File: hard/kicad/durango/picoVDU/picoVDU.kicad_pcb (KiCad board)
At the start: 2 copper layers, 31 parts, among them J1 VIDEO, Q1 BC547B, Q2 BC547B, U1 74HCT93, U10 74HC21, U11 74HC20, U12 74HCT02, U13 74HCT00, U14 74HC175, U15 74HC86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

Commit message: improved picoVDU
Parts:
- added J2: IOX, Connector_PinHeader_2.54mm:PinHeader_2x08_P2.54mm_Vertical, F.Cu at (11.4, 45.7)
- added U19: 74HC32, Package_DIP:DIP-14_W7.62mm_Socket, F.Cu at (4.48, 45.9)
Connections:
- net Net-(U15-Pad3) renamed /ABE
- U15 pad 1: ~ABE -> +5V
- U15 pad 2: +5V -> ~ABE
- U18 pad 1: /Interface/~IO8U -> /Interface/~SEL
- U18 pad 15: /Interface/~IO8Q -> /Interface/~DSEL
- U6 pad 12: Net-(U6-Pad12) -> GND

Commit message: routing picoVDU
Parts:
- J1: footprint Connector_Audio:Jack_3.5mm_Neutrik_NMJ6HCD2_Horizontal -> Connector_Coaxial:SMA_Amphenol_132289_EdgeMount
- moved U19 191.1 mm to (148.6, 171.4), turned to 90 degrees
- moved J2 182.6 mm to (170.2, 135.9)
- moved U6 174.3 mm to (137.2, 143.5), turned to 270 degrees
- moved J1 157.4 mm to (61.0, 174.0), turned to 180 degrees
- moved U13 142.1 mm to (88.9, 151.1), turned to 90 degrees
- moved U9 140.7 mm to (100.3, 171.4)
- moved U7 138.2 mm to (102.9, 184.2), turned to 90 degrees
- moved U15 136.5 mm to (148.6, 184.2), turned to 90 degrees
- moved U18 134.5 mm to (146.1, 158.8), turned to 90 degrees
- moved U14 130.0 mm to (125.7, 184.2), turned to 90 degrees
- moved R4 128.0 mm to (88.9, 171.4)
- moved U1 127.5 mm to (63.5, 133.3), turned to 180 degrees
- moved U12 126.3 mm to (128.3, 171.4), turned to 90 degrees
- moved C2 125.5 mm to (73.7, 174.0), turned to 180 degrees
- moved U8 122.2 mm to (68.6, 151.1), turned to 90 degrees
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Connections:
- J2 pad 10: D1 -> D4
- J2 pad 11: D2 -> /Interface/~SEL
- J2 pad 12: D3 -> D5
- J2 pad 13: D4 -> /Interface/~WE
- J2 pad 14: D5 -> D6
- J2 pad 15: D6 -> GND
- J2 pad 2: /Interface/A0 -> D0
- J2 pad 3: /Interface/A1 -> /Interface/A0
- J2 pad 4: /Interface/A2 -> D1
- J2 pad 5: /Interface/A3 -> /Interface/A1
- J2 pad 6: /Interface/~SEL -> D2
- J2 pad 7: /Interface/~WE -> /Interface/A2
- J2 pad 8: GND -> D3
- J2 pad 9: D0 -> /Interface/A3
- U17 pad 12: INV -> Net-(U17-Pad12)
- U17 pad 16: Net-(U17-Pad16) -> INV
- U3 pad 10: Net-(U10-Pad8) -> Net-(U13-Pad12)
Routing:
- net GND: track 0.00 -> 441.6 mm, vias 0 -> 2
- net +5V: track 0.00 -> 378.9 mm
- net INV: track 0.00 -> 72.7 mm, vias 0 -> 2
- net ~ABE: track 0.00 -> 47.8 mm, vias 0 -> 1
- net /VD1: track 0.00 -> 47.1 mm, vias 0 -> 2
- net /Interface/A1: track 0.00 -> 41.8 mm, vias 0 -> 1
- net D7: track 0.00 -> 37.7 mm
- net D0: track 0.00 -> 37.5 mm
- net /VD2: track 0.00 -> 36.6 mm
- net Net-(U17-Pad11): track 0.00 -> 35.7 mm
- net D6: track 0.00 -> 35.1 mm
- net D1: track 0.00 -> 33.9 mm, vias 0 -> 1
- net Net-(U11-Pad9): track 0.00 -> 32.6 mm
- net D5: track 0.00 -> 28.8 mm, vias 0 -> 1
- net /VD7: track 0.00 -> 28.0 mm
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
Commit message: more routing on picoVDU
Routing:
- net Net-(U10-Pad4): track 0.00 -> 129.7 mm, vias 0 -> 4
- net Net-(U10-Pad12): track 0.00 -> 107.1 mm, vias 0 -> 2
- net +5V: track 378.9 -> 482.4 mm, vias 0 -> 3
- net Net-(U10-Pad2): track 0.00 -> 93.7 mm, vias 0 -> 3
- net Net-(R3-Pad2): track 0.00 -> 82.2 mm
- net Net-(U10-Pad1): track 0.00 -> 79.5 mm, vias 0 -> 2
- net D4: track 26.6 -> 104.2 mm, vias 1 -> 3
- net ~DBE: track 0.00 -> 72.6 mm, vias 0 -> 1
- net D3: track 22.6 -> 93.5 mm, vias 1 -> 3
- net D5: track 28.8 -> 97.1 mm, vias 1 -> 2
- net D2: track 25.7 -> 94.1 mm, vias 1 -> 3
- net VA9: track 0.00 -> 67.5 mm, vias 0 -> 2
- net /Interface/~SEL: track 8.67 -> 74.1 mm, vias 0 -> 2
- net D0: track 37.5 -> 101.4 mm, vias 0 -> 1
- net VA10: track 0.00 -> 62.4 mm, vias 0 -> 2
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
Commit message: almost routed picoVDU
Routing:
- net Net-(U12-Pad5): track 0.00 -> 142.3 mm, vias 0 -> 5
- net Net-(U10-Pad5): track 13.8 -> 137.5 mm, vias 0 -> 5
- net Net-(U13-Pad12): track 0.00 -> 123.5 mm, vias 0 -> 4
- net /ABE: track 13.8 -> 130.1 mm, vias 0 -> 4
- net Net-(U1-Pad8): track 0.00 -> 114.7 mm
- net Net-(U11-Pad13): track 0.00 -> 92.8 mm, vias 0 -> 1
- net Net-(U14-Pad9): track 47.4 -> 113.0 mm, vias 1 -> 2
- net Net-(U11-Pad1): track 0.00 -> 64.9 mm, vias 0 -> 2
- net Net-(U2-Pad9): track 0.00 -> 64.1 mm, vias 0 -> 2
- net Net-(U1-Pad2): track 0.00 -> 60.7 mm, vias 0 -> 3
- net Net-(U13-Pad2): track 11.2 -> 66.4 mm, vias 0 -> 1
- net GND: track 468.2 -> 509.2 mm, vias 2 -> 5
- net VA5: track 33.3 -> 73.9 mm, vias 1 -> 4
- net Net-(U10-Pad9): track 14.8 -> 52.2 mm, vias 0 -> 2
- net Net-(U11-Pad9): track 32.6 -> 69.2 mm, vias 0 -> 2
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
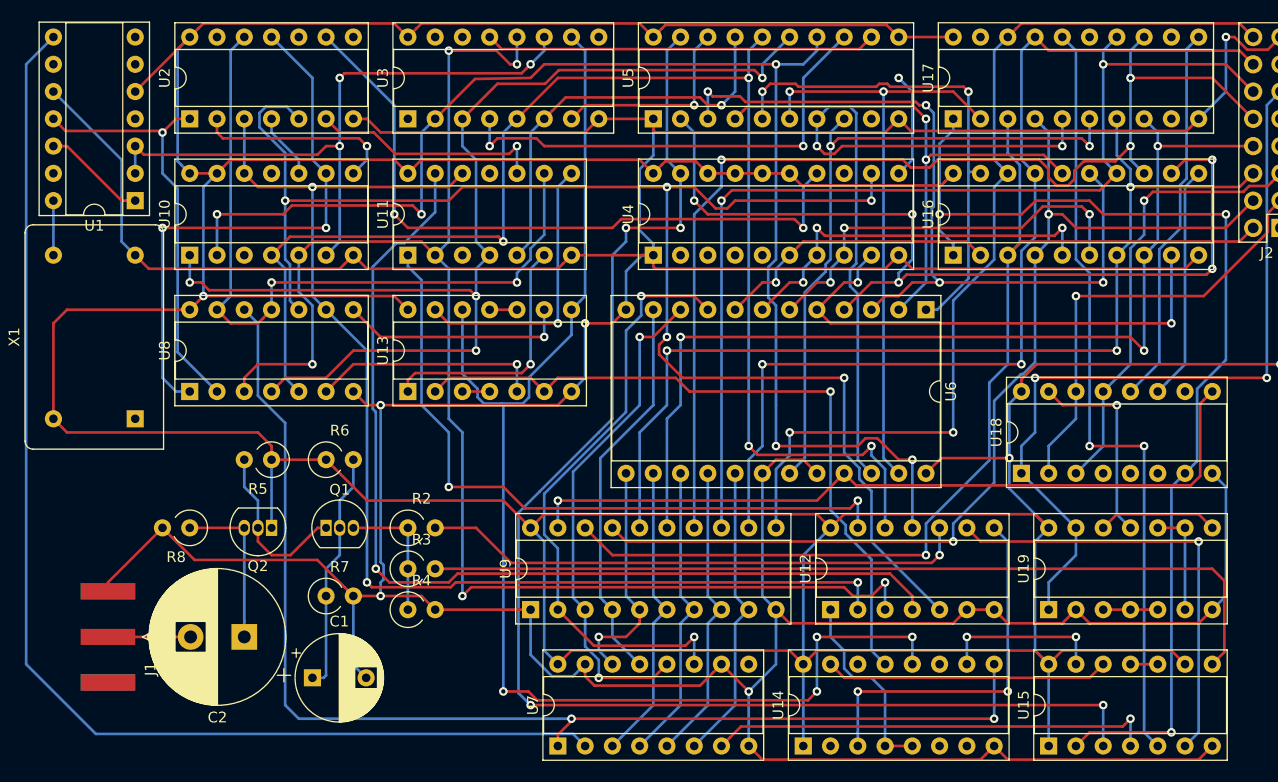
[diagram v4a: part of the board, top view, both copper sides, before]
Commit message: finished routing picoVDU
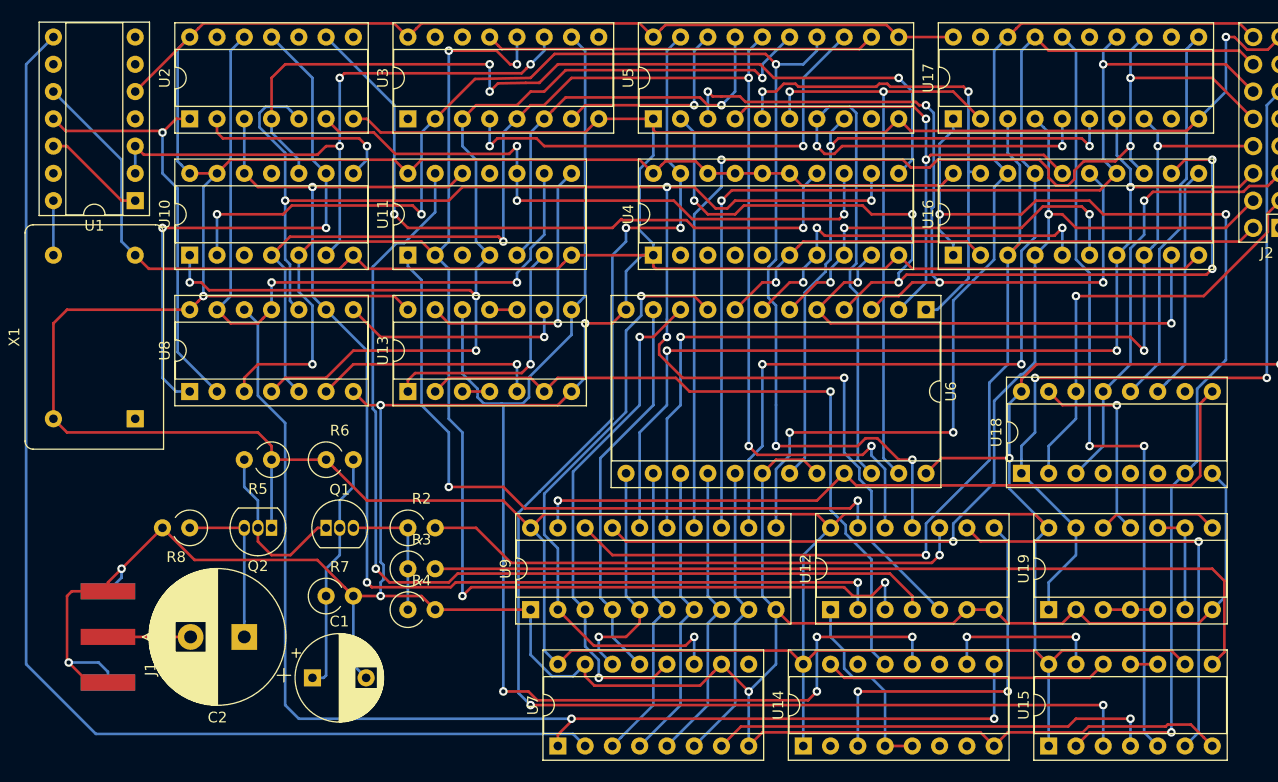
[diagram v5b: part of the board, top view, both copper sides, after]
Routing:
- net Net-(U10-Pad10): track 16.1 -> 82.9 mm, vias 1 -> 3
- net Net-(U11-Pad10): track 22.0 -> 59.7 mm, vias 1 -> 3
- net GND: track 509.2 -> 533.9 mm, vias 5 -> 7
- net VA4: track 86.2 -> 86.9 mm
- net Net-(U10-Pad2): track 129.0 -> 129.6 mm

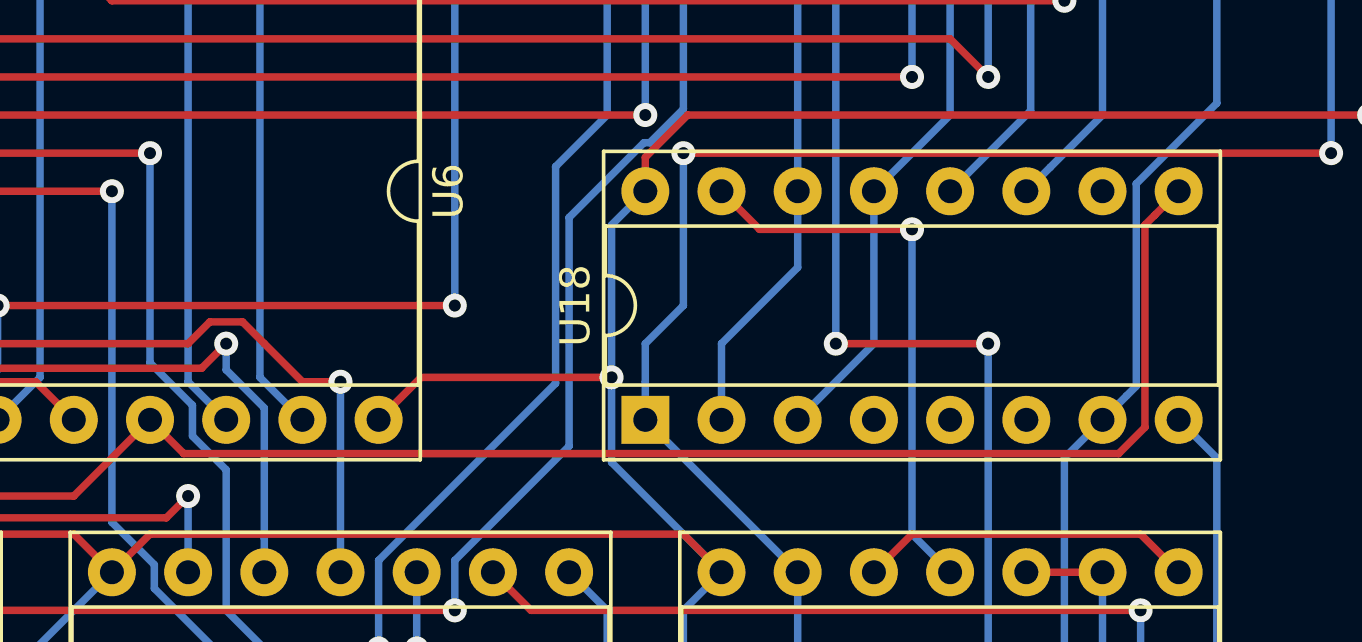
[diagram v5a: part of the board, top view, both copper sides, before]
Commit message: new IO8 address for picoVDU
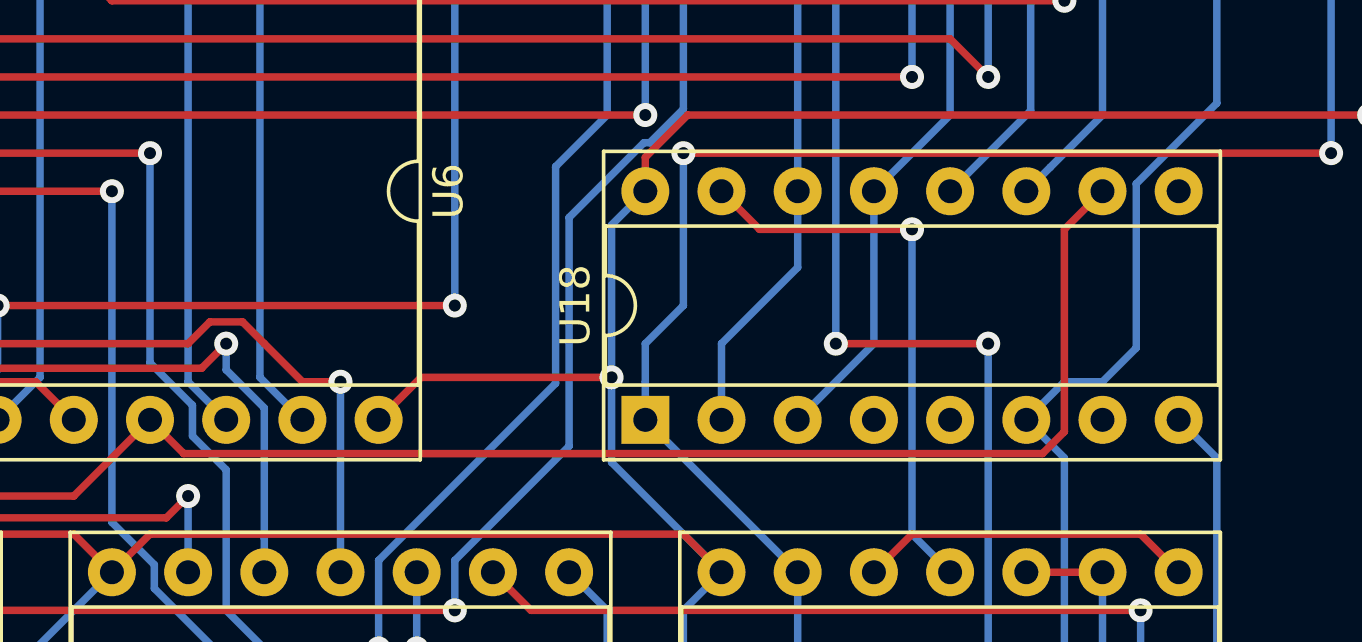
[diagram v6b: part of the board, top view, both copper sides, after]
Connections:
- U18 pad 10: Net-(U18-Pad10) -> ~DBE
- U18 pad 6: Net-(U18-Pad6) -> ~ABE
- U18 pad 7: ~ABE -> Net-(U18-Pad7)
- U18 pad 9: ~DBE -> Net-(U18-Pad9)
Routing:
- net ~DBE: track 72.6 -> 70.1 mm
- net ~ABE: track 101.2 -> 103.0 mm
